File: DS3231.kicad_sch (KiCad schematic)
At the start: 8 parts, among them IC1 DS3231, J1 Conn_01x08_Pin

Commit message: docs: fill in the title block
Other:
- company: (none) -> UHasselt, Solar Cooker
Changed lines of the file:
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@@
 	(title_block
 		(title "DS3231")
-		(date "2024-03-06")
+		(date "2026-09-26")
+		(rev "1.0")
+		(company "UHasselt, Solar Cooker")
+		(comment 1 "Based on the Adafruit DS3231 Precision RTC breakout")
+		(comment 2 "Design: Lowie Van Vyve")
+		(comment 3 "github.com/solar-cooker-UHasselt/kicad-adafruit-ds3231")
 	)
 	(junction

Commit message: fix: use the Keystone 3000 battery holder
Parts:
- B1: footprint external_footprints:CR1220 -> Battery:BatteryHolder_Keystone_3000_1x12mm; MPN 3001 -> 3000; SPN 36-3001-ND -> 36-3000-ND
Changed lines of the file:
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@@
 			)
 		)
-		(property "Footprint" "external_footprints:CR1220"
+		(property "Footprint" "Battery:BatteryHolder_Keystone_3000_1x12mm"
 			(at 184.15 105.156 90)
 			(hide yes)
@@
 			)
 		)
-		(property "MPN" "3001"
+		(property "MPN" "3000"
 			(at 184.15 106.68 0)
 			(hide yes)
@@
 			)
 		)
-		(property "SPN" "36-3001-ND"
+		(property "SPN" "36-3000-ND"
 			(at 184.15 106.68 0)
 			(hide yes)

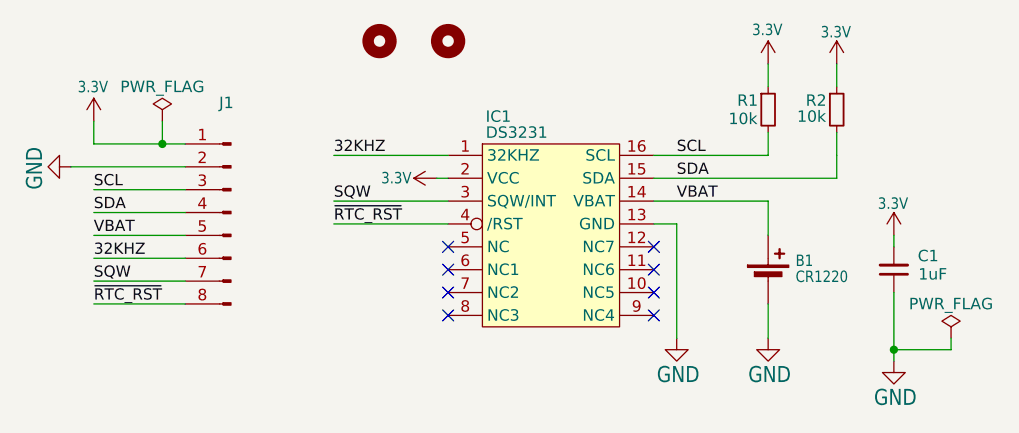
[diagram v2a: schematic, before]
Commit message: fix: ground DS3231 pins 5 to 12
The datasheet says these N.C. pins must be connected to ground, they
were left open. Rename them GND in the symbol, wire them to GND and
connect the pads in the layout.
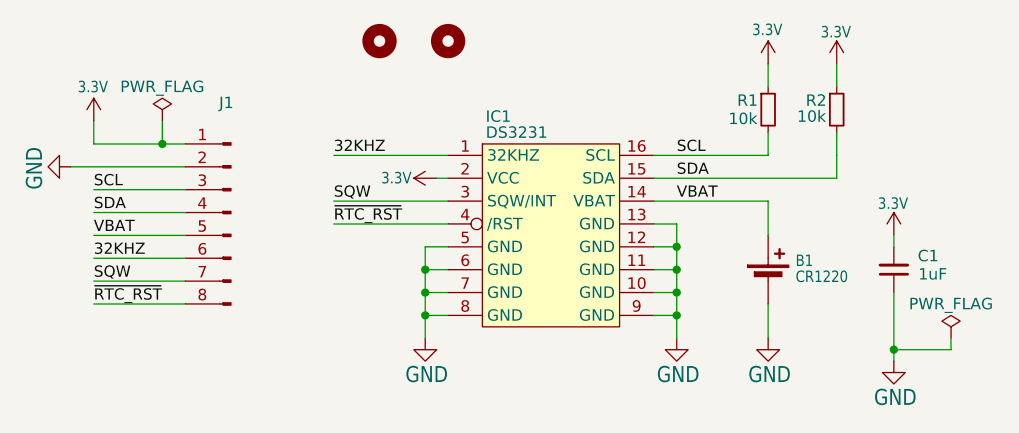
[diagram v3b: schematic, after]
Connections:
- net GND: now also IC1.10 (GND), IC1.11 (GND), IC1.12 (GND), IC1.5 (GND), IC1.6 (GND), IC1.7 (GND), IC1.8 (GND), IC1.9 (GND)
- no-connect marks 8 -> 0

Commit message: build(lib): use the kicad-common library
Own parts now come from the shared kicad-common submodule instead of
copies in external/. IC1 and the logo point to solar_cooker, with the
same netlist and ERC/DRC results.
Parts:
- IC1: symbol external_library:DS3231 -> solar_cooker:DS3231M
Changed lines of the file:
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@@
 	)
 	(symbol
-		(lib_id "external_library:DS3231")
+		(lib_id "solar_cooker:DS3231M")
 		(at 152.4 111.76 0)
 		(unit 1)
